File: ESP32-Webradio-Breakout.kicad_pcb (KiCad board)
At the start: 2 copper layers, 68 x 31 mm, 50 parts, among them J1 AudioJack3, J2 Conn_01x02, P1 USB_C_Plug, Q1 BC817, Q2 BC817, Q3 BC817, SW1 RotaryEncoder_Switch, U1 AMS1117-3.3, U2 ESP32-WROOM-32, U3 CH340C, U4 PCF8574TS, U5 DS18B20

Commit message: Added pin for touch sensor Marked mounting holes as not in schematic
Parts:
- added J2: Conn_01x01, Connector_PinHeader_2.54mm:PinHeader_1x01_P2.54mm_Vertical, F.Cu at (28.9, 37.4)
- renumbered J2 to J3
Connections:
- U2 pad 26: unconnected-(U2-Pad26) -> /Touch_Sens
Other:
- board text added: "TOUCH"
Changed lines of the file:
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@@
   (net 60 "unconnected-(U2-Pad23)")
   (net 61 "unconnected-(U2-Pad24)")
-  (net 62 "unconnected-(U2-Pad26)")
+  (net 62 "/Touch_Sens")
   (net 63 "unconnected-(U2-Pad27)")
   (net 64 "unconnected-(U2-Pad28)")
@@
     (descr "Mounting Hole 3.2mm, M3")
     (tags "mounting hole 3.2mm m3")
-    (attr board_only exclude_from_pos_files exclude_from_bom)
+    (attr board_only exclude_from_bom)
     (fp_text reference "REF**" (at 0 -4.2) (layer "F.SilkS") hide
       (effects (font (size 1 1) (thickness 0.15)))
@@
   (footprint "" (layer "F.Cu")
     (at 28.85 45.8)
+    (attr board_only exclude_from_bom)
     (fp_text reference "" (at 0 0) (layer "F.SilkS")
       (effects (font (size 1.27 1.27) (thickness 0.15)))
@@
     (property "Sheetname" "")
     (attr through_hole)
-    (fp_text reference "J2" (at -2.175 1.15) (layer "F.SilkS")
+    (fp_text reference "J3" (at -2.175 1.15) (layer "F.SilkS")
       (effects (font (size 1 1) (thickness 0.15)))
     )
@@
   (footprint "" (layer "F.Cu")
     (at 89.05 45.8)
+    (attr board_only exclude_from_bom)
     (fp_text reference "" (at 0 0) (layer "F.SilkS")
       (effects (font (size 1.27 1.27) (thickness 0.15)))
@@
       (net 36 "/IO0") (pinfunction "IO0") (pintype "bidirectional"))
     (pad "26" smd rect (at 8.5 6.985 180) (size 2 0.9) (layers "F.Cu" "F.Paste" "F.Mask")
-      (net 62 "unconnected-(U2-Pad26)") (pinfunction "IO4") (pintype "bidirectional+no_connect"))
+      (net 62 "/Touch_Sens") (pinfunction "IO4") (pintype "bidirectional"))
     (pad "27" smd rect (at 8.5 5.715 180) (size 2 0.9) (layers "F.Cu" "F.Paste" "F.Mask")
       (net 63 "unconnected-(U2-Pad27)") (pinfunction "IO16") (pintype "bidirectional+no_connect"))
@@
   (footprint "" (layer "F.Cu")
     (at 28.85 28.85)
+    (attr board_only exclude_from_bom)
     (fp_text reference "" (at 0 0) (layer "F.SilkS")
       (effects (font (size 1.27 1.27) (thickness 0.15)))
@@
     )
   )
+  (footprint "Connector_PinHeader_2.54mm:PinHeader_1x01_P2.54mm_Vertical" (layer "F.Cu")
+    (at 28.85 37.35)
+    (descr "Through hole straight pin header, 1x01, 2.54mm pitch, single row")
+    (tags "Through hole pin header THT 1x01 2.54mm single row")
+    (property "Sheetfile" "ESP32-Webradio-Breakout.kicad_sch")
+    (property "Sheetname" "")
+    (attr through_hole)
+    (fp_text reference "J2" (at -0.05 2.2) (layer "F.SilkS")
+      (effects (font (size 1 1) (thickness 0.15)))
+    )
+    (fp_text value "Conn_01x01" (at 0 2.33) (layer "F.Fab")
+      (effects (font (size 1 1) (thickness 0.15)))
+    )
+    (fp_text user "${REFERENCE}" (at 0 0 90) (layer "F.Fab")
+      (effects (font (size 1 1) (thickness 0.15)))
+    )
+    (fp_line (start -1.33 -1.33) (end 0 -1.33) (layer "F.SilkS") (width 0.12))
+    (fp_line (start -1.33 1.27) (end -1.33 1.33) (layer "F.SilkS") (width 0.12))
+    (fp_line (start -1.33 0) (end -1.33 -1.33) (layer "F.SilkS") (width 0.12))
+    (fp_line (start -1.33 1.27) (end 1.33 1.27) (layer "F.SilkS") (width 0.12))
+    (fp_line (start 1.33 1.27) (end 1.33 1.33) (layer "F.SilkS") (width 0.12))
+    (fp_line (start -1.33 1.33) (end 1.33 1.33) (layer "F.SilkS") (width 0.12))
+    (fp_line (start 1.8 1.8) (end 1.8 -1.8) (layer "F.CrtYd") (width 0.05))
+    (fp_line (start -1.8 -1.8) (end -1.8 1.8) (layer "F.CrtYd") (width 0.05))
+    (fp_line (start -1.8 1.8) (end 1.8 1.8) (layer "F.CrtYd") (width 0.05))
+    (fp_line (start 1.8 -1.8) (end -1.8 -1.8) (layer "F.CrtYd") (width 0.05))
+    (fp_line (start -1.27 1.27) (end -1.27 -0.635) (layer "F.Fab") (width 0.1))
+    (fp_line (start 1.27 1.27) (end -1.27 1.27) (layer "F.Fab") (width 0.1))
+    (fp_line (start 1.27 -1.27) (end 1.27 1.27) (layer "F.Fab") (width 0.1))
+    (fp_line (start -0.635 -1.27) (end 1.27 -1.27) (layer "F.Fab") (width 0.1))
+    (fp_line (start -1.27 -0.635) (end -0.635 -1.27) (layer "F.Fab") (width 0.1))
+    (pad "1" thru_hole rect (at 0 0) (size 1.7 1.7) (drill 1) (layers *.Cu *.Mask)
+      (net 62 "/Touch_Sens") (pinfunction "Pin_1") (pintype "passive"))
+    (model "${KICAD6_3DMODEL_DIR}/Connector_PinHeader_2.54mm.3dshapes/PinHeader_1x01_P2.54mm_Vertical.wrl"
+      (offset (xyz 0 0 0))
+      (scale (xyz 1 1 1))
+      (rotate (xyz 0 0 0))
+    )
+  )
   (footprint "Package_SO:SOIC-16_3.9x9.9mm_P1.27mm" (layer "F.Cu")
     (at 116.03 28.67)
@@
   (gr_line (start 93 25) (end 93 56) (layer "Edge.Cuts") (width 0.1))
   (gr_line (start 25 56) (end 25 25) (layer "Edge.Cuts") (width 0.1))
+  (gr_text "TOUCH" (at 31 37.35 90) (layer "B.SilkS")
+    (effects (font (size 1 1) (thickness 0.15)) (justify mirror))
+  )
   (gr_text "SDA" (at 76.15 29.225 90) (layer "B.SilkS")
     (effects (font (size 1 1) (thickness 0.15)) (justify mirror))
@@
     )
   )
+  (group "Touch" (id 5107c977-189f-4c7f-aca4-81c5ab8d4859)
+    (members
+      0b407da0-92a2-4325-8a96-2a5c720c93b1
+      f698f53d-0378-4128-b32d-0d8d90618ce9
+    )
+  )

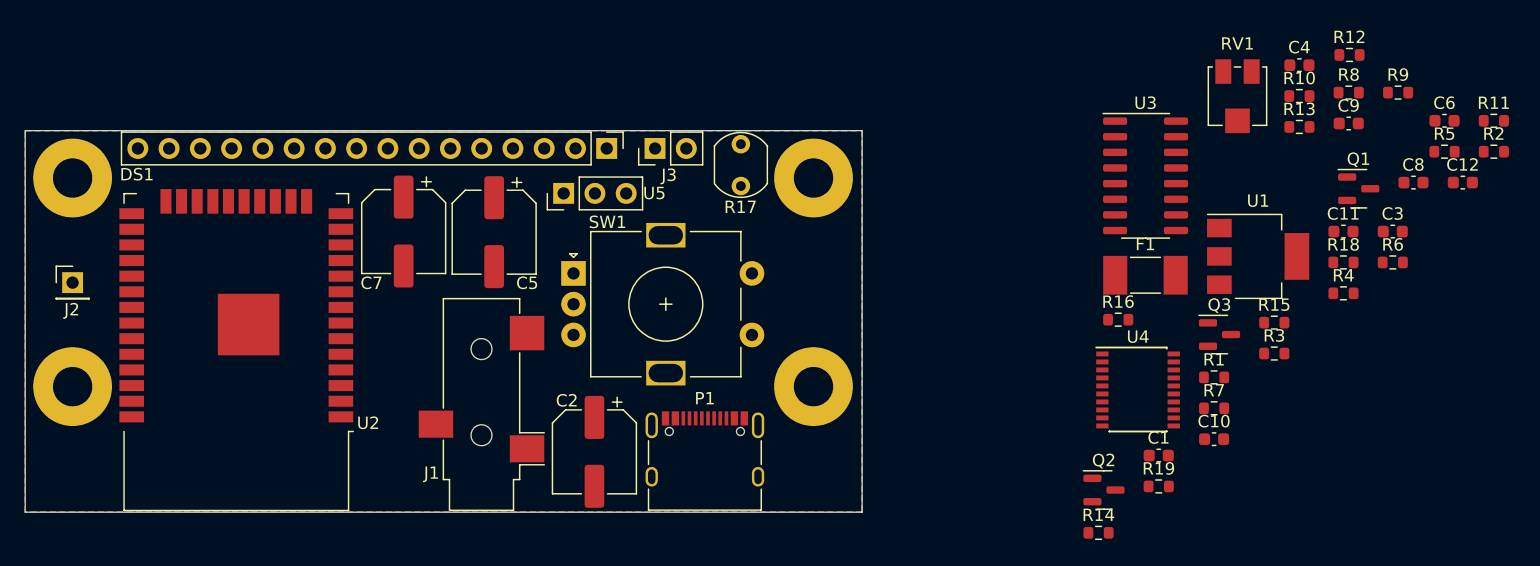
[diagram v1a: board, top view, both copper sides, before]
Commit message: Changed USB-C symbol Added 5k1 resistors for 5V handshake
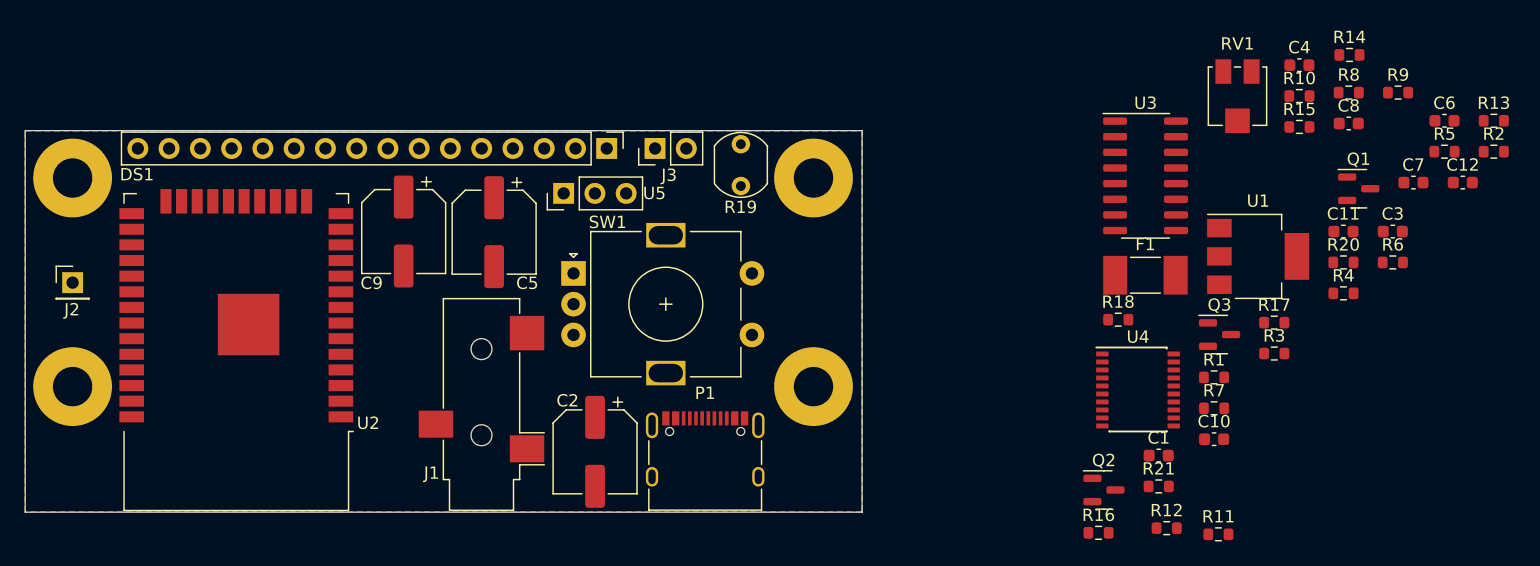
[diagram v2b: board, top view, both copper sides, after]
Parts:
- added R11: 5k1, Resistor_SMD:R_0603_1608Metric, F.Cu at (122.0, 57.8)
- added R12: 5k1, Resistor_SMD:R_0603_1608Metric, F.Cu at (117.8, 57.3)
- renumbered C8 to C7, C9 to C8, C7 to C9, R11 to R13, R12 to R14, R13 to R15, R14 to R16, R15 to R17, R16 to R18, R17 to R19, R18 to R20, R19 to R21
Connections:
- P1 pad A5: unconnected-(P1-PadA5) -> Net-(P1-PadA5)
- P1 pad A6: Net-(P1-PadA6) -> unconnected-(P1-PadA6)
- P1 pad A7: Net-(P1-PadA7) -> unconnected-(P1-PadA7)
- P1 pad B5: unconnected-(P1-PadB5) -> Net-(P1-PadB5)
- P1 pad B6: (no net) -> Net-(P1-PadB6)
- P1 pad B7: (no net) -> Net-(P1-PadB7)
- U3 pad 5: Net-(P1-PadA6) -> Net-(P1-PadB6)
- U3 pad 6: Net-(P1-PadA7) -> Net-(P1-PadB7)

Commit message: first routing
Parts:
- C1, C10, C11, C12, C3, C4, C6, C7, C8, F1, Q1, Q2, Q3, R1, R10, R11, R12, R13, R14, R15, R16, R17, R18, R2, R20, R21, R3, R4, R5, R6, R7, R8, R9, RV1, U1, U3, U4: moved to B.Cu
- moved U4 71.5 mm to (44.6, 36.6), turned to 180 degrees
- moved C3 55.6 mm to (80.5, 34.6)
- moved C4 53.6 mm to (80.5, 43.5)
- moved U1 48.3 mm to (77.0, 39.1)
- moved F1 46.8 mm to (71.3, 50.7), turned to 90 degrees
- moved R13 42.4 mm to (102.1, 27.8), turned to 180 degrees
- moved R2 32.7 mm to (111.7, 26.7), turned to 180 degrees
- moved R16 31.6 mm to (143.8, 57.7), turned to 180 degrees
- moved Q2 30.7 mm to (143.4, 54.2), turned to 180 degrees
- moved R18 28.4 mm to (142.2, 40.4), turned to 180 degrees
- moved C12 27.6 mm to (114.2, 29.2), turned to 180 degrees
- moved C6 24.6 mm to (115.7, 24.2), turned to 180 degrees
- moved R5 24.6 mm to (115.7, 26.7), turned to 180 degrees
- moved C1 21.8 mm to (138.9, 51.4), turned to 180 degrees
- moved R21 21.8 mm to (138.9, 53.9), turned to 180 degrees
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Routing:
- net /SCL: track 0.00 -> 54.5 mm, vias 0 -> 1
- net /SDA: track 0.00 -> 52.5 mm, vias 0 -> 1
- net Net-(DS1-Pad5): track 0.00 -> 28.4 mm
- net /P2: track 0.00 -> 25.9 mm
- net VCC: track 0.00 -> 22.9 mm, vias 0 -> 1
- net Net-(F1-Pad1): track 0.00 -> 20.3 mm, vias 0 -> 1
- net Net-(DS1-Pad11): track 0.00 -> 12.4 mm
- net +3V3: track 0.00 -> 10.9 mm
- net Net-(DS1-Pad12): track 0.00 -> 10.7 mm
- net Net-(DS1-Pad13): track 0.00 -> 9.61 mm
- net Net-(DS1-Pad14): track 0.00 -> 9.35 mm
- net /TXD: track 0.00 -> 8.81 mm
- net /RXD: track 0.00 -> 8.14 mm

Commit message: routing
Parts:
- moved R16 100.4 mm to (45.3, 37.9)
- moved Q3 95.5 mm to (38.9, 33.2)
- moved R7 90.5 mm to (45.4, 31.5)
- moved R1 85.2 mm to (49.2, 45.5)
- moved R21 83.8 mm to (55.7, 43.5)
- moved R14 82.7 mm to (44.5, 43.7)
- moved R17 79.6 mm to (49.9, 39.6)
- moved R15 78.4 mm to (50.2, 38.0)
- moved R3 74.3 mm to (55.4, 38.1)
- moved R6 70.4 mm to (49.6, 32.0)
- moved R18 69.1 mm to (74.2, 28.3)
- moved RV1 68.4 mm to (65.0, 33.3), turned to 0 degrees
- moved R13 68.0 mm to (34.4, 34.2)
- moved R8 65.2 mm to (58.9, 30.4)
- moved R2 63.6 mm to (49.9, 41.8)
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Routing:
- net /IO0: track 0.00 -> 92.3 mm, vias 0 -> 1
- net /RXD: track 8.14 -> 67.2 mm, vias 0 -> 1
- net /TXD: track 8.81 -> 58.9 mm, vias 0 -> 1
- net VCC: track 22.9 -> 65.0 mm, vias 1 -> 2
- net Net-(P1-PadB7): track 0.00 -> 19.5 mm, vias 0 -> 1
- net Net-(P1-PadB6): track 0.00 -> 15.2 mm, vias 0 -> 1
- net Net-(DS1-Pad3): track 0.00 -> 5.53 mm
- net +3V3: track 10.9 -> 15.6 mm
- net Net-(Q2-Pad2): track 0.00 -> 3.00 mm
- net /Temp_Sens: track 0.00 -> 2.78 mm
- net /SDA: track 52.5 -> 49.8 mm
- net Net-(Q2-Pad1): track 0.00 -> 2.03 mm
- net /Light_Sens: track 0.00 -> 1.96 mm
- net /SCL: track 54.5 -> 52.6 mm
- net Net-(C5-Pad1): track 0.00 -> 1.45 mm
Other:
- board size 68 x 31 mm -> 70 x 31 mm

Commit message: routing
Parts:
- moved Q2 54.8 mm to (38.4, 38.5), turned to 90 degrees
- moved R10 52.3 mm to (38.4, 41.3), turned to 0 degrees
- moved Q1 51.9 mm to (41.9, 38.5), turned to 90 degrees
- moved R9 48.7 mm to (41.8, 41.3), turned to 0 degrees
- moved C11 41.2 mm to (45.9, 33.2)
- moved U3 35.7 mm to (54.2, 34.6), turned to 180 degrees
- moved C6 34.9 mm to (52.9, 44.4), turned to 0 degrees
- moved C1 31.6 mm to (52.9, 47.5)
- moved C8 28.8 mm to (49.0, 30.1)
- moved C7 25.7 mm to (59.5, 34.0), turned to 0 degrees
- moved R21 23.3 mm to (37.8, 28.6), turned to 0 degrees
- moved R7 22.3 mm to (60.2, 48.0)
- moved R2 19.8 mm to (69.5, 44.4), turned to 90 degrees
- moved R6 18.0 mm to (60.2, 46.5)
- moved C10 15.8 mm to (66.9, 29.8), turned to -90 degrees
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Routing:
- net /IO0: track 92.3 -> 0.00 mm, vias 1 -> 0
- net /RXD: track 67.2 -> 0.00 mm, vias 1 -> 0
- net VCC: track 65.0 -> 2.53 mm, vias 2 -> 0
- net /TXD: track 58.9 -> 0.00 mm, vias 1 -> 0
- net /SCL: track 52.6 -> 2.44 mm, vias 1 -> 0
- net /SDA: track 49.8 -> 2.34 mm, vias 1 -> 0
- net Net-(DS1-Pad5): track 28.4 -> 0.00 mm
- net /P2: track 25.9 -> 0.00 mm
- net Net-(F1-Pad1): track 20.3 -> 0.00 mm, vias 1 -> 0
- net Net-(P1-PadB7): track 19.5 -> 0.00 mm, vias 1 -> 0
- net Net-(P1-PadB6): track 15.2 -> 0.00 mm, vias 1 -> 0
- net /Enc_SW: track 0.00 -> 13.7 mm
- net Net-(DS1-Pad11): track 12.4 -> 0.00 mm
- net Net-(DS1-Pad12): track 10.7 -> 0.00 mm
- net Net-(DS1-Pad13): track 9.61 -> 0.00 mm
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
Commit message: Parts placement
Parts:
- moved R6 3.56 mm to (60.5, 43.0)
- moved R7 3.51 mm to (60.5, 44.5)
- moved R8 3.31 mm to (60.5, 41.5)
- moved R5 3.26 mm to (60.5, 39.9)
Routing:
- net /Enc_SW: track 13.7 -> 0.00 mm
- net +3V3: track 10.7 -> 0.00 mm, vias 1 -> 0
- net /Enc_A: track 7.57 -> 0.00 mm
- net /EN: track 4.80 -> 0.00 mm, vias 2 -> 0
- net Net-(R17-Pad2): track 4.04 -> 0.00 mm
- net Net-(R16-Pad2): track 3.68 -> 0.00 mm
- net Net-(R15-Pad2): track 2.86 -> 0.00 mm
- net VCC: track 2.53 -> 0.00 mm
- net /SCL: track 2.44 -> 0.00 mm
- net /SDA: track 2.34 -> 0.00 mm
- net /Temp_Sens: track 2.03 -> 0.00 mm
- net /Light_Sens: track 1.96 -> 0.00 mm
- net /Enc_B: track 1.92 -> 0.00 mm
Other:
- board size 70 x 31 mm -> 68 x 31 mm
